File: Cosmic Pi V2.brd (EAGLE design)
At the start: 239.4 x 121.7 mm, 191 parts, among them IC1 AD8039, IC2 AD8039, IC3 LP2985IM5-3.1, IC4 LM555D, IC5 LM555D, IC6 LM555D, IC7 74AUC1G00DBV, IC8 74AUC1G00DBV, IC9 74AUC1G00DBV, J1 U.FL-R-SMT-1(10), J10 2p-2.54, J11 2p-2.54, J2 U.FL-R-SMT-1(10), J3 4p-2.54, J4 4p-2.54, J5 5-1814400-1, J6 2p-2.54, J7 2p-2.54, J8 2p-2.54, J9 2p-2.54, Q1 BSS123, Q2 BSS123, U1 L76-M33, U2 LSM303D, U5 MAX1932, U6 MAX1932, X1 22-23-2041, X2 22-23-2041, X3 22-23-2021, X4 22-23-2051

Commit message: Work in progress
Added DACs.
Tidied Sheet 1 - Analogue.
Started Adding STM32's (one of two).
To do: 1 - 1mm2 SiPM Footprint
2 - Finish STM32s (2)
3- Power regulator + jack
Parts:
- removed DUE1: DUE(NORMAL), DUElib130425:DUE(NORMAL)
- removed J3, J4: 4p-2.54, Seeed-Connector:H4-2.54
- removed J6: 2p-2.54, Seeed-Connector:H2-2.54
- removed X1: 22-23-2041, con-molex:22-23-2041
- removed X3: 22-23-2021, con-molex:22-23-2021
- added C65, C66: 100n, resistor:C0603
- added C67, C68: 10u, resistor:C0603
- added C69, C70: 20p, rcl:C0603
- added C71: 4.7u, resistor:C0603
- added U$10: 310010495_STM32F401RET6, Seeed-OPL-2017-01-IC-Akita:LQFP64
- added U3, U4: MCP4725, SparkFun-IC-Conversion:SOT23-6
- X2: value 22-23-2041 -> 306010282_XTAL_8MHZ-HC49US; device con-molex:22-23-2041 -> Seeed-OPL-2017-01-Crystal-Akita:HC49UP
- moved X2 321.5 mm to (-9.00, -266.0), flipped to the top, turned to 0 degrees
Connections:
- removed net AMP2B: DUE1.A7, IC$3.5, J3.1
- removed net DREF1: DUE1.A1
- removed net DREF2: DUE1.A2
- removed net EXTGPSFIX: DUE1.4
- removed net HTU3V: DUE1.9
- removed net IMU3V: DUE1.8
- removed net N$12: R4.2, R5.2, X3.2
- removed net PA0: DUE1.A9
- removed net PA1: DUE1.A10
- removed net PA2: DUE1.A11
- removed net TEMPA: J6.1
- removed net TEMPB: J6.2
- new net +5FV: C7.1, IC3.1, IC3.3, L1.2, R6.1
- new net AGND: C11.2, C14.2, C15.2, C19.2, C2.2, C20.2, C21.2, C22.2, C24.2, C25.2, C3.2, C6.-, C7.2, C8.2, IC1.4, IC2.4, IC3.2, L1.3, LED1.C, LED2.C, R32.1
- new net N$21: U$10.P$12
- new net N$49: U$10.P$31
- new net N$51: U$10.P$47
- new net N$62: C71.2, U$10.P$30
- new net TEMP1: R4.1, R5.1
- new net TEMP2: R4.2, R5.2
- new net VBAT: U$10.P$1
- new net VDD1: U$10.P$32
- new net VDD2: U$10.P$48
- net !RESET: no longer DUE1.RESET
- net +3V3: now also U$10.P$13, U$10.P$19, U$10.P$64; no longer DUE1.3V3
- net +5V: no longer C7.1, DUE1.5V, IC3.1, IC3.3, J4.1, L1.2, R6.1
- net ACCELINT1: no longer DUE1.10
- net ACCELINT2: no longer DUE1.13
- net ACCELINT3: no longer DUE1.SDA1
- net ACCELSA0: no longer DUE1.6
- net ACCELSA1: no longer DUE1.7
- net AMP2A: no longer DUE1.A6, J3.3
- net GND: now also C65.1, C66.1, C67.1, C68.1, C69.1, C71.1, L1.4, U$10.P$18, U$10.P$63, U3.2, U4.2, U4.6; no longer C11.2, C14.2, C15.2, C19.2, C2.2, C20.2, C21.2, C22.2, C24.2, C25.2, C3.2, C6.-, C7.2, C8.2, DUE1.GND1, DUE1.GND_1, DUE1.GND_2, DUE1.GND_A, DUE1.GND_B, IC1.4, IC2.4, IC3.2, J3.2, J4.2, L1.3, LED1.C, LED2.C, R32.1, X1.3
- net GPSPPS: no longer DUE1.2
- net GPSRX: no longer DUE1.TX1
- net GPSTX: no longer DUE1.RX1
- net LED1: no longer DUE1.12
- net LED2: no longer DUE1.11
- net LEDB: no longer DUE1.A8, J3.4, X1.1
- net MAX1932!CL: no longer DUE1.3
- net MAX1932!CS1: no longer DUE1.TX3
- net MAX1932!CS2: no longer DUE1.RX3
- net MAX1932DIN: no longer DUE1.TX2
- net MAX1932SCLK: no longer DUE1.RX2
- net N$1: no longer X2.4
- net N$2: now also C69.2, U$10.P$5, X2.P$1; no longer L1.4, X2.3
- net N$8: now also C70.2, U$10.P$6, X2.P$2; no longer R4.1, R5.1, X3.1
- net PSUF1: now also C65.2, C66.2, C67.2, C68.2, U3.3, U3.6, U4.3
- net RX0: no longer DUE1.RX0
- net SCL0: now also U3.5, U4.5; no longer DUE1.SCL
- net SDA0: now also U3.4, U4.4; no longer DUE1.SDA
- net SIG2A: no longer X1.2
- net SIG2B: now also IC$3.5; no longer X1.4
- net STRIGAOUT: no longer DUE1.A5
- net STRIGBOUT: no longer DUE1.A0
- net TRIGOUT: no longer DUE1.5
- net TX0: no longer DUE1.TX0
- net UCDAC0: now also U3.1; no longer DUE1.DAC0
- net UCDAC1: now also U4.1; no longer DUE1.DAC1
- net VBIAS1: no longer J4.3, X2.2
- net VBIAS2: no longer J4.4, X2.1
- net VBIASFB1: no longer DUE1.A3
- net VBIASFB2: no longer DUE1.A4
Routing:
- net N$12: track 108.5 -> 0.00 mm, vias 1 -> 0
- net TEMP2: track 0.00 -> 106.6 mm, vias 0 -> 1
- net N$8: track 99.2 -> 0.00 mm, vias 1 -> 0
- net TEMP1: track 0.00 -> 97.3 mm, vias 0 -> 1
- net +5V: track 13.6 -> 0.00 mm
- net +5FV: track 0.00 -> 12.2 mm
- net SIG2A: track 6.87 -> 0.99 mm
- net N$2: track 4.74 -> 0.00 mm
- net SIG2B: track 26.0 -> 21.3 mm
- net GND: track 0.00 -> 2.68 mm
- net N$1: track 8.06 -> 6.22 mm
- net VBIAS2: track 93.2 -> 91.9 mm
- net VBIAS1: track 97.3 -> 96.0 mm

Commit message: Updated schematic - nearly finished
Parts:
- removed J10, J11: 2p-2.54, Seeed-Connector:H2-2.54
- removed R44, R45, R46: 1M, resistor:R0603
- removed R48: 24.9k, resistor:R0603
- removed R51: 15k, resistor:R0603
- removed SIPM1, SIPM1_TOP, SIPM2, SIPM2_TOP: (no value), diode:ASD-NUV3S-P
- removed U5, U6: MAX1932, TQFN-12:TQFN-12
- removed X4: 22-23-2051, con-molex:22-23-2051
- added C72, C75: 1n, rcl:C0603
- added C73, C74, C76: 100n, resistor:C0603
- added C77, C78: 20p, rcl:C0603
- added C79: 4.7u, resistor:C0603
- added D6: CD1206-S01575, diode:MINIMELF
- added D7, D8: SS1P3L, SmartPrj:DO220AAL
- added IC10: AD8039, Cosmic Pi V2:ANALOG-DEVICES_SO8
- added IC11: 24C00OT, microchip:SOT23-5L
- added IC12: NCP1117ST33T3G -3V3, linear:SOT223
- added IC13: LM2734Y, SmartPrj:SOT23-6
- added J12, J13, J15, J16: 2p-2.54, Seeed-Connector:H2-2.54
- added J14, J6: 2X4P-2.54, Seeed-Connector:H2X4-2.54
- added J3, J4: BNCPTH, SparkFun-Connectors:BNC
- added L10: MH2029-300Y, wuerth-elektronik:0805
- added L11: 10u SRR0604-100ML, SmartPrj:SRR0604
- added PC1, PC2: 47u, rcl:PANASONIC_D
- added PI_GPIO: (no value), con-lstb:MA20-2
- added R64, R73: 100, rcl:R0603
- added R65, R74: 500k, rcl:R0603
- added R66, R75: 1M, rcl:R0603
- added R67, R68: 10K, rcl:R0805
- added R69, R72: 0 ohm, rcl:R1206
- added R70, R76: DNP, rcl:R0603
- added R71, R77: 50k, rcl:R0603
- added SIPM1X1_BOT, SIPM1X1_TOP: (no value), Cosmic Pi V2:DIODE_ASD-NUV1S-P
- added SIPM3X3_BOT, SIPM3X3_TOP: (no value), Cosmic Pi V2:DIODE_ASD-NUV3S-P
- added U$11: 310010495_STM32F401RET6, Seeed-OPL-2017-01-IC-Akita:LQFP64
- added U$9: UCC27528UCC27528DR, Cosmic Pi V2:ANALOG-DEVICES_SO8
- added X1: POWERSUPPLY_DC21MMX, SmartPrj:POWERSUPPLY_DC-21MM
- added X3: 306010282_XTAL_8MHZ-HC49US, Seeed-OPL-2017-01-Crystal-Akita:HC49UP
- C10: value 220n -> 100n; device rcl:C0603 -> resistor:C0603
- C45: value 220n -> 10u; device rcl:C0603 -> rcl:SMC_B
- C47: value 1u -> 10u; device resistor:C0603 -> rcl:SMC_B
- C48: value 100n -> 10n; device resistor:C0603 -> SmartPrj:C0603-ROUND
- R10: value 1M -> 806
- R12: value 15k -> 806
- R13: value 1M -> 10k; device resistor:R0603 -> SmartPrj:R0402
- R14: value 1M -> 10K; device resistor:R0603 -> SmartPrj:R0603-ROUND
- R19: value 24.9k -> 52K3; device resistor:R0603 -> SmartPrj:R0603-ROUND
- moved C48 436.0 mm to (-103.0, -567.0)
- moved R19 421.0 mm to (-114.0, -568.0)
- moved C45 409.5 mm to (-84.0, -550.0)
- moved R14 403.7 mm to (-108.0, -568.0)
- moved R13 397.6 mm to (-98.0, -567.0)
- moved C47 376.0 mm to (-79.0, -550.0)
- moved C10 312.2 mm to (-128.0, -458.0)
- moved R12 282.3 mm to (-129.0, -426.0)
- moved R10 275.4 mm to (-129.0, -421.0)
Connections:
- removed net !RESET: X4.4
- removed net MAX1932!CL: U5.3, U6.3
- removed net MAX1932!CS1: R10.2, U5.12
- removed net MAX1932!CS2: R44.2, U6.12
- removed net MAX1932DIN: R14.2, R46.2, U5.2, U6.2
- removed net MAX1932SCLK: R13.2, R45.2, U5.1, U6.1
- removed net N$17: BAT46WH1.1, C9.1, R20.2, U5.4
- removed net N$35: R51.1, U6.8
- removed net N$36: C45.1, R51.2
- removed net N$37: R48.2, R49.1, R50.2, U6.7
- removed net N$54: R19.1, U5.6
- removed net N$56: C10.1, R12.2
- removed net RX0: X4.3
- removed net TX0: X4.2
- removed net VBAT: U$10.P$1
- removed net VDD1: U$10.P$32
- removed net VDD2: U$10.P$48
- new net +4.1V: R67.1
- new net BOOST: C48.1, D6.C, IC13.1
- new net BOOT1: PI_GPIO.7, U$10.P$60
- new net BOOT2: PI_GPIO.11, U$11.P$60
- new net EN: IC13.4, R13.2
- new net FB: IC13.3, R14.1, R19.2
- new net HV1EN: U$9.1
- new net HV1PWM: U$10.P$41, U$9.2
- new net HV2EN: U$9.8
- new net HV2PWM: U$10.P$42, U$9.4
- new net ID_SC: IC11.1, PI_GPIO.28
- new net ID_SD: IC11.3, PI_GPIO.27
- new net N$12: C72.1, IC10.3, R64.2, R65.1
- new net N$52: C73.1, IC10.2, R69.2
- new net N$59: C75.1, IC10.5, R73.2, R74.1
- new net N$75: BAT46WH1.1, C9.1, R20.2
- new net N$76: J3.GND, R71.1
- new net N$77: C75.2, IC10.7, R74.2, R75.1
- new net N$79: C77.2, U$11.P$5, X3.P$1
- new net N$80: C74.1, IC10.6, R72.2
- new net N$81: C78.2, U$11.P$6, X3.P$2
- new net N$82: U$11.P$12
- new net N$83: U$11.P$31
- new net N$84: U$11.P$47
- new net N$85: C79.2, U$11.P$30
- new net NRST1: J12.1, U$10.P$7
- new net NRST2: U$11.P$7
- new net PSUFB1: R11.2, R21.1, U$10.P$14
- new net PSUFB2: R49.1, R50.2, U$10.P$15
- new net RESET: PI_GPIO.18
- new net SCL1: PI_GPIO.5
- new net SLOWAOUT: J3.S, R66.2, U$11.P$14
- new net SLOWBOUT: J4.S, R75.2, U$11.P$15
- new net SLOWCHA: C16.2, R26.1, R64.1
- new net SLOWCHB: C1.2, R17.1, R73.1
- new net SPI1_CLK: J13.2, U$11.P$21
- new net SPI1_MISO: U$10.P$22, U$11.P$22
- new net SPI1_MOSI: U$10.P$23, U$11.P$23
- new net SPI_CE0: PI_GPIO.24
- new net SPI_CE1: PI_GPIO.26
- new net STAGE3_DC_OFFSET: R67.2, R68.2, R69.1, R72.1
- new net SW: C48.2, D7.P$1, IC13.6, L11.P$1
- new net TCK: PI_GPIO.23
- new net TCK/SWCLK1: J6.4, U$10.P$49
- new net TCK/SWCLK2: J14.4, U$11.P$49
- new net TDI: PI_GPIO.19
- new net TDI1: J6.6, U$10.P$50
- new net TDI2: J14.6, U$11.P$50
- new net TDO: PI_GPIO.21
- new net TDO/SWO1: J13.1, J6.5, U$10.P$55
- new net TDO/SWO2: J14.5, U$11.P$55
- new net TMS: PI_GPIO.22
- new net TMS/SWIDO1: J6.3, U$10.P$46
- new net TMS/SWIDO2: J14.3, U$11.P$46
- new net TRST1: J12.2, J6.7, U$10.P$56
- new net TRST2: J14.7, U$11.P$56
- new net VIN: C47.+, D8.P$1, IC13.5, PC1.+, R13.1
- new net VIN+: L10.2, X1.2
- net +3V3: now also C10.2, C45.+, IC11.5, IC12.2, IC12.4, J14.1, J6.1, U$10.P$1, U$10.P$32, U$10.P$48, U$11.P$1, U$11.P$13, U$11.P$19, U$11.P$32, U$11.P$48, U$11.P$64
- net +4V: now also C76.1, IC10.8
- net +5V: now also D6.A, IC12.3, L11.P$2, PC2.+, PI_GPIO.2, PI_GPIO.4, R19.1, U$9.6; no longer C47.1, C48.1, R10.1, R44.1, U5.11, U6.11, X4.1
- net ACCELINT1: now also U$11.P$9
- net ACCELINT2: now also U$11.P$10
- net ACCELINT3: now also U$11.P$11
- net ACCELSA0: now also U$11.P$24
- net ACCELSA1: now also U$11.P$25
- net AGND: now also C73.2, C74.2, C76.2, IC10.4, R68.1, R70.1, R71.2, R76.1, R77.2
- net GND: now also C10.1, C45.-, C47.-, C70.1, C77.1, C78.1, C79.1, D7.P$2, IC11.2, IC12.1, IC13.2, J14.2, J14.8, J6.2, J6.8, PC1.-, PC2.-, PI_GPIO.14, PI_GPIO.20, PI_GPIO.25, PI_GPIO.30, PI_GPIO.34, PI_GPIO.39, PI_GPIO.6, PI_GPIO.9, R14.2, U$11.P$18, U$11.P$63, U$9.3, X1.1, X1.3; no longer C10.2, C45.2, C47.2, C48.2, J10.2, J11.2, R13.1, R14.1, R45.1, R46.1, U5.9, U6.9, X4.5
- net GPSRX: now also PI_GPIO.8
- net GPSTX: now also PI_GPIO.10
- net LEDB: now also U$10.P$21; no longer J10.1, J11.1
- net N$18: now also SIPM1X1_TOP.P$1, SIPM3X3_TOP.P$1; no longer SIPM1.P$1, SIPM1_TOP.P$1
- net N$19: now also R10.1; no longer U5.10
- net N$24: now also J4.GND, R77.1; no longer C1.2, R17.1
- net N$27: now also R12.1; no longer U6.10
- net N$30: no longer U6.4
- net N$32: now also C72.2, IC10.1, R65.2, R66.1; no longer C16.2, R26.1
- net N$34: now also R12.2, U$9.5; no longer R48.1, U6.6
- net N$47: now also R10.2, U$9.7; no longer R11.2, R19.2, R21.1, U5.7
- net N$55: now also D8.P$2, L10.1; no longer R12.1, U5.8
- net N$7: now also SIPM1X1_BOT.P$1, SIPM3X3_BOT.P$1; no longer SIPM2.P$1, SIPM2_TOP.P$1
- net SDA0: now also PI_GPIO.3
- net SIG1A: now also SIPM1X1_TOP.P$2, SIPM3X3_TOP.P$2; no longer SIPM1.P$2, SIPM1_TOP.P$2
- net SIG1B: now also SIPM1X1_BOT.P$2, SIPM3X3_BOT.P$2; no longer SIPM2.P$2, SIPM2_TOP.P$2
- net STRIGAOUT: now also U$11.P$43
- net STRIGBOUT: now also U$11.P$44
- net TRIGOUT: now also U$11.P$41
- net VBIAS1: no longer U5.5
- net VBIAS2: no longer U6.5
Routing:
- net SIG1B: track 25.5 -> 20.4 mm
- net SLOWCHA: track 0.00 -> 2.15 mm
- net N$32: track 2.15 -> 0.00 mm
- net SLOWCHB: track 0.00 -> 2.15 mm
- net N$24: track 2.15 -> 0.00 mm

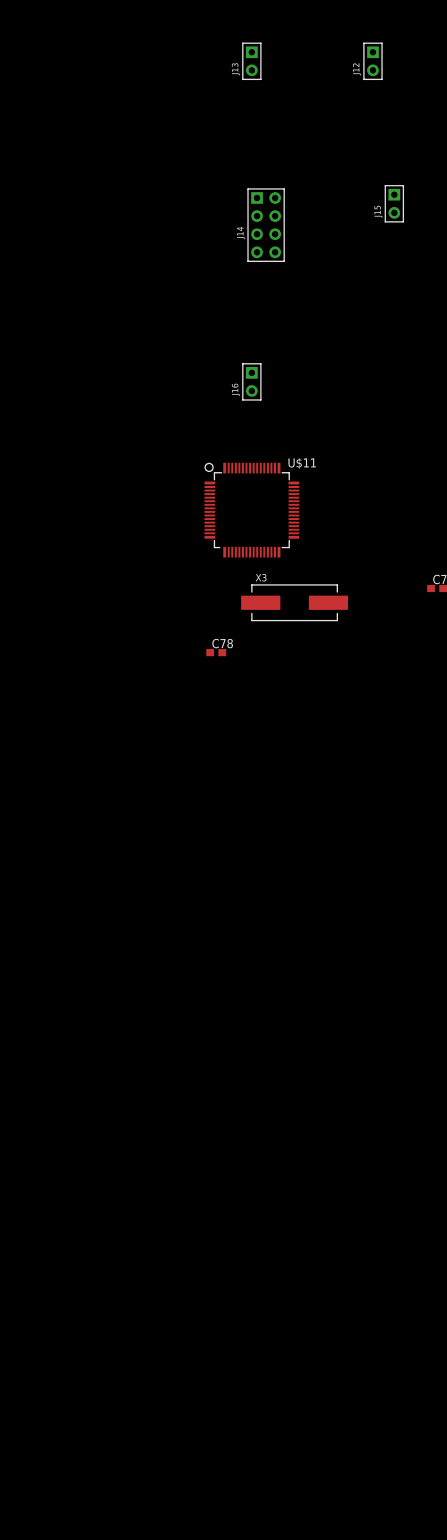
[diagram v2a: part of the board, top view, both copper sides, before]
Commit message: Schematic design completed.
PSU + CPU outputs changed a little after reading the STM32 manual
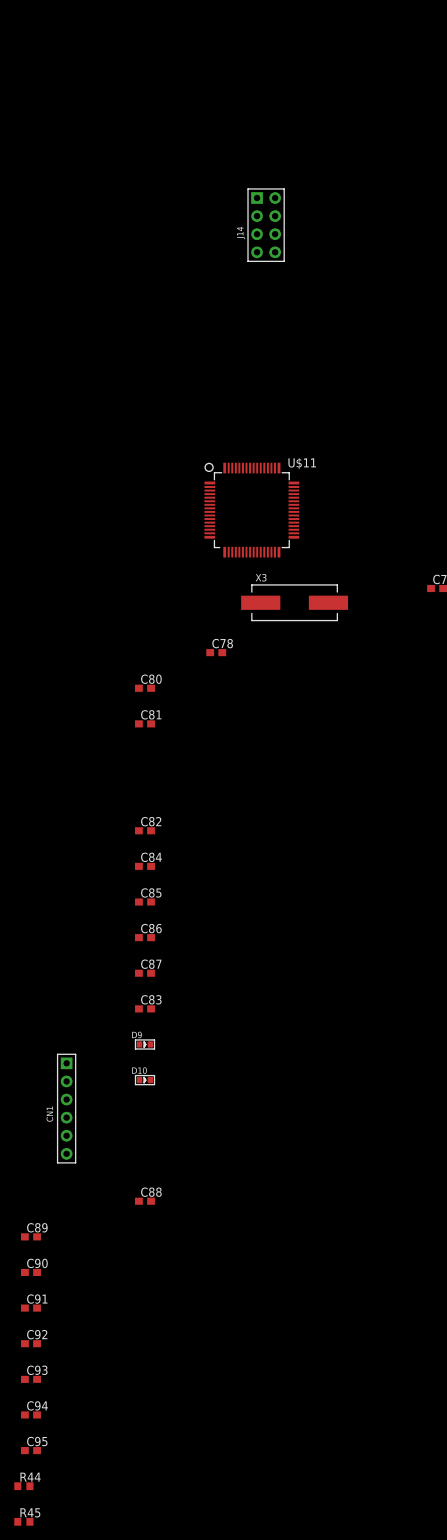
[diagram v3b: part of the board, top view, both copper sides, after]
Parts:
- removed J12, J13, J15, J16: 2p-2.54, Seeed-Connector:H2-2.54
- added C80, C81, C82, C84, C85, C86, C88, C90, C91, C92, C93, C94: 100n, resistor:C0603
- added C83, C95: 1u, resistor:C0603
- added C87, C89: 4.7u, resistor:C0603
- added CN1: 6p-2.54, Seeed-Connector:H6-2.54
- added D10, D9: GREEN-0603, Seeed-LED:LED-0603
- added R44, R45: 40, resistor:R0603
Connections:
- net TCK/SWCLK1 renamed PSU_JTCK-SWCLK
- net TCK/SWCLK2 renamed CPU_JTCK-SWCLK
- net TDI1 renamed PSU_SYS_JTDI
- net TDI2 renamed CPU_SYS_JTDI
- net TMS/SWIDO1 renamed PSU_JTMS-SWDIO
- net TMS/SWIDO2 renamed CPU_JTMS-SWDIO
- net TRST2 renamed CPU_SYS_JTRST
- removed net +4.1V: R67.1
- removed net AMP2A: IC$3.3
- removed net BOOT1: PI_GPIO.7, U$10.P$60
- removed net BOOT2: PI_GPIO.11, U$11.P$60
- removed net N$82: U$11.P$12
- removed net N$83: U$11.P$31
- removed net N$84: U$11.P$47
- removed net NRST1: J12.1, U$10.P$7
- removed net NRST2: U$11.P$7
- removed net RESET: PI_GPIO.18
- removed net SCL1: PI_GPIO.5
- removed net SPI1_CLK: J13.2, U$11.P$21
- removed net SPI1_MISO: U$10.P$22, U$11.P$22
- removed net SPI1_MOSI: U$10.P$23, U$11.P$23
- removed net TCK: PI_GPIO.23
- removed net TDI: PI_GPIO.19
- removed net TDO: PI_GPIO.21
- removed net TDO/SWO1: J13.1, J6.5, U$10.P$55
- removed net TDO/SWO2: J14.5, U$11.P$55
- removed net TMS: PI_GPIO.22
- removed net TRST1: J12.2, J6.7, U$10.P$56
- new net CPU_BOOT0: PI_GPIO.18, U$11.P$60
- new net CPU_JTDO-SWO: J14.8, U$11.P$55
- new net CPU_NRST: C88.1, J14.5, PI_GPIO.16, U$11.P$7
- new net N$35: D9.+, R45.2
- new net N$36: R45.1, U$10.P$8
- new net N$54: R44.1, U$11.P$8
- new net N$71: C91.1, C95.1, U$11.P$13
- new net N$78: C89.1, C90.1, U$11.P$1, U$11.P$19
- new net PI_FLAG0: PI_GPIO.7, U$11.P$39
- new net PI_FLAG1: PI_GPIO.12, U$11.P$40
- new net PI_FLAG2: PI_GPIO.15, U$11.P$51
- new net PSU_BOOT0: PI_GPIO.13
- new net PSU_JTDO-SWO: J6.8, U$10.P$55
- new net PSU_NRST: C80.1, J6.5, PI_GPIO.11, U$10.P$7
- new net PSU_SYS_JTRST: J6.7, U$10.P$56
- new net SPI_CLK: PI_GPIO.23, U$10.P$21, U$11.P$21
- new net SPI_MISO: PI_GPIO.21, U$10.P$22, U$11.P$22
- new net SPI_MOSI: PI_GPIO.19, U$10.P$23, U$11.P$23
- new net USER_0: CN1.3, U$11.P$52
- new net USER_1: CN1.4, U$11.P$53
- new net USER_2: CN1.5, U$11.P$2
- new net USER_3: CN1.6, U$11.P$3
- net +3V3: now also C81.1, C82.1, C83.1, C84.1, C85.1, C86.1, C87.1, CN1.1; no longer U$11.P$1, U$11.P$13, U$11.P$19, U$11.P$32, U$11.P$48, U$11.P$64
- net +4V: now also R67.1
- net +5V: now also L1.1
- net ACCELINT1: now also U$11.P$11; no longer U$11.P$9
- net ACCELINT2: now also U$11.P$24; no longer U$11.P$10
- net ACCELINT3: now also U$11.P$25; no longer U$11.P$11
- net ACCELSA0: now also U$11.P$37; no longer U$11.P$24
- net ACCELSA1: now also U$11.P$38; no longer U$11.P$25
- net GND: now also C80.2, C81.2, C82.2, C83.2, C84.2, C85.2, C86.2, C87.2, C88.2, C89.2, C90.2, C91.2, C92.2, C93.2, C94.2, C95.2, CN1.2, D10.-, D9.-, U$10.P$12, U$10.P$31, U$10.P$47, U$11.P$12, U$11.P$31, U$11.P$47; no longer J14.8, J6.8
- net GPSPPS: now also U$11.P$41
- net HV1EN: now also U$10.P$9
- net HV1PWM: now also U$10.P$14; no longer U$10.P$41
- net HV2EN: now also U$10.P$10
- net HV2PWM: now also U$10.P$17; no longer U$10.P$42
- net LED1: now also U$11.P$9
- net LED2: now also U$11.P$10
- net LEDB: now also U$10.P$41; no longer U$10.P$21
- net N$1: now also D10.+, R44.2; no longer L1.1
- net N$21: now also C94.1, U$11.P$64; no longer U$10.P$12
- net N$49: now also C93.1, U$11.P$48; no longer U$10.P$31
- net N$51: now also C92.1, U$11.P$32; no longer U$10.P$47
- net PSUFB1: now also U$10.P$15; no longer U$10.P$14
- net PSUFB2: now also U$10.P$16; no longer U$10.P$15
- net SCL0: now also PI_GPIO.5
- net SIG2A: now also IC$3.3
- net SLOWAOUT: now also R70.2, U$11.P$15; no longer U$11.P$14
- net SLOWBOUT: now also R76.2, U$11.P$16; no longer U$11.P$15
- net SPI_CE0: now also U$11.P$20
- net SPI_CE1: now also U$10.P$20
- net TRIGOUT: now also U$11.P$42; no longer U$11.P$41
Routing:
- net N$1: track 6.22 -> 0.00 mm
- net +5V: track 0.00 -> 6.22 mm

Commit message: schematic complete, layout tweaks and routing required
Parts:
- removed C48: 10n, SmartPrj:C0603-ROUND
- removed PI_GPIO: (no value), con-lstb:MA20-2
- removed U$10, U$11: 310010495_STM32F401RET6, Seeed-OPL-2017-01-IC-Akita:LQFP64
- added CPU, PSU: 310010495_STM32F401RET6, Seeed-OPL-2017-01-IC-Akita:LQFP64
- added LED3: top-mounted, eagle-ltspice:LED_SML0603
- added LED4: bottom-mounted, eagle-ltspice:LED_SML0603
- added R46: top-mounted, rcl:R0402
- added R48: bottom-mounted, rcl:R0402
- added U$12: RPI-ZERO, RPI-Zero:RASPBERRYPI_BASTELSTUBE_V13_RASPI_BOARD_B+_FULL
- added USB1: 10118193-0001LF, Seeed-Connector:MICRO-USB5+6P-SMD-0.65-B
- J3, J4: value BNCPTH -> 5-1814400-1_5-1814400-1; device SparkFun-Connectors:BNC -> Cosmic Pi V2:5-1814400-1_TE_5-1814400-1
- R13: value 10k -> 10K; device SmartPrj:R0402 -> Seeed-Resistor:R0603
- R14: device SmartPrj:R0603-ROUND -> Seeed-Resistor:R0603
- R19: value 52K3 -> 51K; device SmartPrj:R0603-ROUND -> Seeed-Resistor:R0603
- moved R44 832.2 mm to (92.8, 15.0)
- moved C95 828.0 mm to (85.8, 18.5), flipped to the bottom
- moved C94 818.4 mm to (85.8, 13.2), flipped to the bottom
- moved R45 818.1 mm to (32.2, 16.0), turned to 270 degrees
- moved C93 816.3 mm to (85.8, 16.0), flipped to the bottom
- moved C92 813.7 mm to (83.0, 19.2), flipped to the bottom, turned to 270 degrees
- moved C91 805.6 mm to (80.0, 16.8), flipped to the bottom, turned to 180 degrees
- moved C90 798.4 mm to (80.0, 14.0), flipped to the bottom, turned to 180 degrees
- moved C89 794.0 mm to (82.8, 13.2), flipped to the bottom, turned to 90 degrees
- moved C88 785.8 mm to (91.0, 12.5), turned to 270 degrees
- moved D10 775.6 mm to (93.5, 17.5), turned to 90 degrees
- moved CN1 770.0 mm to (82.1, 7.62), turned to 90 degrees
- moved C83 751.1 mm to (42.0, 20.0), flipped to the bottom, turned to 270 degrees
- moved D9 746.6 mm to (31.2, 13.8), turned to 180 degrees
- moved C87 745.7 mm to (38.5, 20.5), flipped to the bottom, turned to 180 degrees
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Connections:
- new net 5V0@2: U$12.2, U$12.4
- new net GND@3: U$12.25, U$12.39, U$12.9
- new net GND@7: U$12.14, U$12.20, U$12.30, U$12.34, U$12.6
- net +3V3: now also PSU.P$1, PSU.P$13, PSU.P$19, PSU.P$32, PSU.P$48, PSU.P$64; no longer U$10.P$1, U$10.P$13, U$10.P$19, U$10.P$32, U$10.P$48, U$10.P$64
- net +5V: now also USB1.1; no longer PI_GPIO.2, PI_GPIO.4
- net ACCELINT1: now also CPU.P$11; no longer U$11.P$11
- net ACCELINT2: now also CPU.P$24; no longer U$11.P$24
- net ACCELINT3: now also CPU.P$25; no longer U$11.P$25
- net ACCELSA0: now also CPU.P$37; no longer U$11.P$37
- net ACCELSA1: now also CPU.P$38; no longer U$11.P$38
- net AGND: now also LED3.C, LED4.C
- net BOOST: no longer C48.1
- net CPU_BOOT0: now also CPU.P$60, U$12.18; no longer PI_GPIO.18, U$11.P$60
- net CPU_JTCK-SWCLK: now also CPU.P$49; no longer U$11.P$49
- net CPU_JTDO-SWO: now also CPU.P$55; no longer U$11.P$55
- net CPU_JTMS-SWDIO: now also CPU.P$46; no longer U$11.P$46
- net CPU_NRST: now also CPU.P$7, U$12.16; no longer PI_GPIO.16, U$11.P$7
- net CPU_SYS_JTDI: now also CPU.P$50; no longer U$11.P$50
- net CPU_SYS_JTRST: now also CPU.P$56; no longer U$11.P$56
- net GND: now also CPU.P$12, CPU.P$18, CPU.P$31, CPU.P$47, CPU.P$63, PSU.P$12, PSU.P$18, PSU.P$31, PSU.P$47, PSU.P$63, USB1.5, USB1.S1, USB1.S2, USB1.S3, USB1.S4, USB1.S5, USB1.S6; no longer PI_GPIO.14, PI_GPIO.20, PI_GPIO.25, PI_GPIO.30, PI_GPIO.34, PI_GPIO.39, PI_GPIO.6, PI_GPIO.9, U$10.P$12, U$10.P$18, U$10.P$31, U$10.P$47, U$10.P$63, U$11.P$12, U$11.P$18, U$11.P$31, U$11.P$47, U$11.P$63
- net GPSPPS: now also CPU.P$41; no longer U$11.P$41
- net GPSRX: now also U$12.8; no longer PI_GPIO.8
- net GPSTX: now also U$12.10; no longer PI_GPIO.10
- net HV1EN: now also PSU.P$9; no longer U$10.P$9
- net HV1PWM: now also PSU.P$14; no longer U$10.P$14
- net HV2EN: now also PSU.P$10; no longer U$10.P$10
- net HV2PWM: now also PSU.P$17; no longer U$10.P$17
- net ID_SC: now also U$12.28; no longer PI_GPIO.28
- net ID_SD: now also U$12.27; no longer PI_GPIO.27
- net LED1: now also CPU.P$9; no longer U$11.P$9
- net LED2: now also CPU.P$10; no longer U$11.P$10
- net LEDB: now also PSU.P$41; no longer U$10.P$41
- net N$2: now also PSU.P$5; no longer U$10.P$5
- net N$20: now also LED3.A
- net N$21: now also CPU.P$64; no longer U$11.P$64
- net N$24: now also J4.1; no longer J4.GND
- net N$3: now also LED4.A
- net N$36: now also PSU.P$8; no longer U$10.P$8
- net N$49: now also CPU.P$48; no longer U$11.P$48
- net N$51: now also CPU.P$32; no longer U$11.P$32
- net N$54: now also CPU.P$8; no longer U$11.P$8
- net N$62: now also PSU.P$30; no longer U$10.P$30
- net N$71: now also CPU.P$13; no longer U$11.P$13
- net N$76: now also J3.1; no longer J3.GND
- net N$78: now also CPU.P$1, CPU.P$19; no longer U$11.P$1, U$11.P$19
- net N$79: now also CPU.P$5; no longer U$11.P$5
- net N$8: now also PSU.P$6; no longer U$10.P$6
- net N$81: now also CPU.P$6; no longer U$11.P$6
- net N$85: now also CPU.P$30; no longer U$11.P$30
- net PI_FLAG0: now also CPU.P$39, U$12.7; no longer PI_GPIO.7, U$11.P$39
- net PI_FLAG1: now also CPU.P$40, U$12.12; no longer PI_GPIO.12, U$11.P$40
- net PI_FLAG2: now also CPU.P$51, U$12.15; no longer PI_GPIO.15, U$11.P$51
- net PSUFB1: now also PSU.P$15; no longer U$10.P$15
- net PSUFB2: now also PSU.P$16; no longer U$10.P$16
- net PSU_BOOT0: now also U$12.13; no longer PI_GPIO.13
- net PSU_JTCK-SWCLK: now also PSU.P$49; no longer U$10.P$49
- net PSU_JTDO-SWO: now also PSU.P$55; no longer U$10.P$55
- net PSU_JTMS-SWDIO: now also PSU.P$46; no longer U$10.P$46
- net PSU_NRST: now also PSU.P$7, U$12.11; no longer PI_GPIO.11, U$10.P$7
- net PSU_SYS_JTDI: now also PSU.P$50; no longer U$10.P$50
- net PSU_SYS_JTRST: now also PSU.P$56; no longer U$10.P$56
- net SCL0: now also U$12.5; no longer PI_GPIO.5
- net SDA0: now also U$12.3; no longer PI_GPIO.3
- net SLOWAOUT: now also CPU.P$15, J3.5; no longer J3.S, U$11.P$15
- net SLOWBOUT: now also CPU.P$16, J4.5; no longer J4.S, U$11.P$16
- net SPI_CE0: now also CPU.P$20, U$12.24; no longer PI_GPIO.24, U$11.P$20
- net SPI_CE1: now also PSU.P$20, U$12.26; no longer PI_GPIO.26, U$10.P$20
- net SPI_CLK: now also CPU.P$21, PSU.P$21, U$12.23; no longer PI_GPIO.23, U$10.P$21, U$11.P$21
- net SPI_MISO: now also CPU.P$22, PSU.P$22, U$12.21; no longer PI_GPIO.21, U$10.P$22, U$11.P$22
- net SPI_MOSI: now also CPU.P$23, PSU.P$23, U$12.19; no longer PI_GPIO.19, U$10.P$23, U$11.P$23
- net STRIGAOUT: now also CPU.P$43; no longer U$11.P$43
- net STRIGBOUT: now also CPU.P$44; no longer U$11.P$44
- net SW: no longer C48.2
- net TEMP1: now also R46.1, R48.1
- net TEMP2: now also R46.2, R48.2
- net TRIGOUT: now also CPU.P$42; no longer U$11.P$42
- net USER_0: now also CPU.P$52; no longer U$11.P$52
- net USER_1: now also CPU.P$53; no longer U$11.P$53
- net USER_2: now also CPU.P$2; no longer U$11.P$2
- net USER_3: now also CPU.P$3; no longer U$11.P$3
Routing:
- net GND: track 2.68 -> 664.9 mm, vias 57 -> 29
- net +3V3: track 0.00 -> 491.5 mm, vias 0 -> 17
- net AGND: track 0.00 -> 278.8 mm, vias 0 -> 14
- net SPI_MISO: track 0.00 -> 240.7 mm, vias 0 -> 4
- net +5V: track 6.22 -> 241.3 mm, vias 0 -> 16
- net STRIGB: track 0.00 -> 229.3 mm, vias 0 -> 1
- net GPSPPS: track 0.00 -> 187.4 mm, vias 0 -> 5
- net SDA0: track 0.00 -> 185.8 mm, vias 0 -> 7
- net SLOWBOUT: track 0.00 -> 174.3 mm, vias 0 -> 4
- net SCL0: track 0.00 -> 146.3 mm, vias 0 -> 12
- net SPI_CLK: track 0.00 -> 138.0 mm, vias 0 -> 10
- net PSU_NRST: track 0.00 -> 132.8 mm, vias 0 -> 6
- net CPU_NRST: track 0.00 -> 132.5 mm, vias 0 -> 4
- net GPSRX: track 0.00 -> 127.0 mm, vias 0 -> 2
- net HV2EN: track 0.00 -> 122.1 mm, vias 0 -> 2
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- removed copper zone on layer 1, net N$14
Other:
- board size 239.4 x 121.7 mm -> 120 x 159.8 mm
- board text removed: "+V_s"
- board text removed: "A"
- board text removed: "CosmicPi Analog Frontend V 2.5 NB'17"
- board text removed: "GND"
- board text removed: "GND_s"
- board text removed: "HV A B"
- board text removed: "K"
- board text removed: "LED"
- board text removed: "Released under CERN OHL V1.2"
- board text removed: "SIG A"
- board text removed: "SIG B"
- board text removed: "T sensor"
